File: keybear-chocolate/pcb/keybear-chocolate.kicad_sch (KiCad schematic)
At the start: 107 parts, among them J2 BATT, J3 LED, J4 OLED, P1 USB_C_Plug, SW1 SW_PUSH, SW10 SW_PUSH, SW11 SW_PUSH, SW12 SW_PUSH, SW13 SW_PUSH, SW14 SW_PUSH, SW15 SW_PUSH, SW16 SW_PUSH, SW17 SW_PUSH, SW18 SW_PUSH, SW19 SW_PUSH, SW2 SW_PUSH, SW20 SW_PUSH, SW21 SW_PUSH, SW22 SW_PUSH, SW25 Rotary_Encoder_Switch, SW3 SW_PUSH, SW30 BATT_SW, SW4 SW_PUSH, SW5 SW_PUSH, SW6 SW_PUSH, SW7 SW_PUSH, SW8 SW_PUSH, SW9 SW_PUSH, U1 ProMicro, U2 MCP23017_ML, U3 ATECC608A-SSHDA

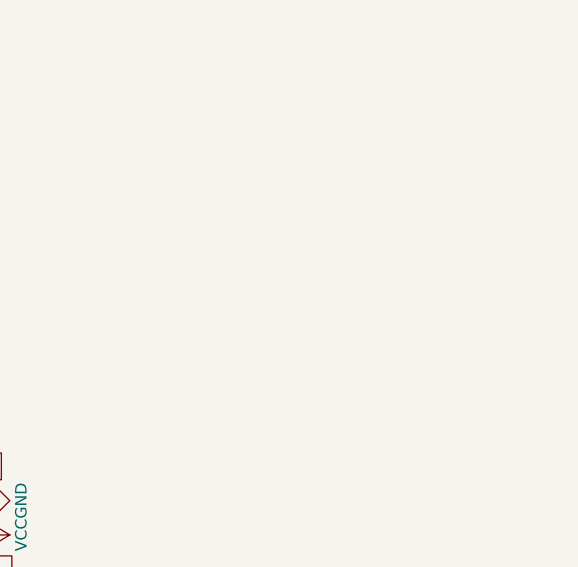
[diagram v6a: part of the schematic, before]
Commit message: adding PCF8523 (Real Time Clock)
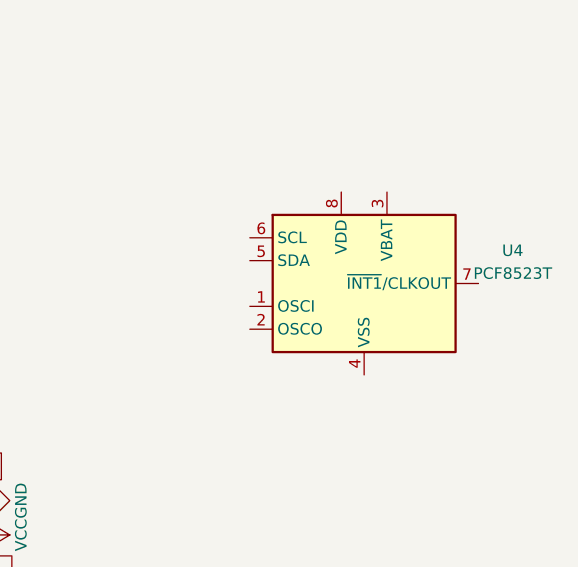
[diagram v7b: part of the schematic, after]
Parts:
- added U4: PCF8523T, Package_SO:SOIC-8_3.9x4.9mm_P1.27mm, symbol Timer_RTC:PCF8523T
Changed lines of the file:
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@@
+    )
+  )
+  (symbol (lib_id "Timer_RTC:PCF8523T") (at 318.77 101.6 0) (unit 1)
+    (in_bom yes) (on_board yes) (dnp no) (fields_autoplaced)
+    (property "Reference" "U4" (at 335.28 97.9521 0)
+      (effects (font (size 1.27 1.27)))
+    )
+    (property "Value" "PCF8523T" (at 335.28 100.4921 0)
+      (effects (font (size 1.27 1.27)))
+    )
+    (property "Footprint" "Package_SO:SOIC-8_3.9x4.9mm_P1.27mm" (at 339.09 110.49 0)
+      (effects (font (size 1.27 1.27)) hide)
+    )
+    (property "Datasheet" "https://www.nxp.com/docs/en/data-sheet/PCF8523.pdf" (at 318.77 101.6 0)
+      (effects (font (size 1.27 1.27)) hide)
+    )
+    (pin "1")
+    (pin "2")
+    (pin "3")
+    (pin "4")
+    (pin "5")
+    (pin "6")
+    (pin "7")
+    (pin "8")
+    (instances
+      (project "keybear-chocolate"
+        (path "/b2404ab0-025a-473e-9fbb-0abc932972cf"
+          (reference "U4") (unit 1)
+        )
+      )
     )
   )

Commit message: creating connections for the rtc and crypto chip
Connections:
- net GND: now also U3.4 (GND), U4.4 (VSS)
- net SCL: now also U3.6 (SCL), U4.6 (SCL)
- net SDA: now also U3.5 (SDA), U4.5 (SDA)
- net VCC: now also U3.8 (VCC), U4.8 (VDD)
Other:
- moved on the sheet: J4, SW25, U3, U4
